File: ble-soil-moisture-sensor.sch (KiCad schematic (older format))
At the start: 29 parts, among them P1 CONN_02X03, Q1 Q_NMOS_GSD, Q2 Q_PMOS_GSD, Q3 Q_PMOS_GSD, U1 BGM111, U2 TPS78225

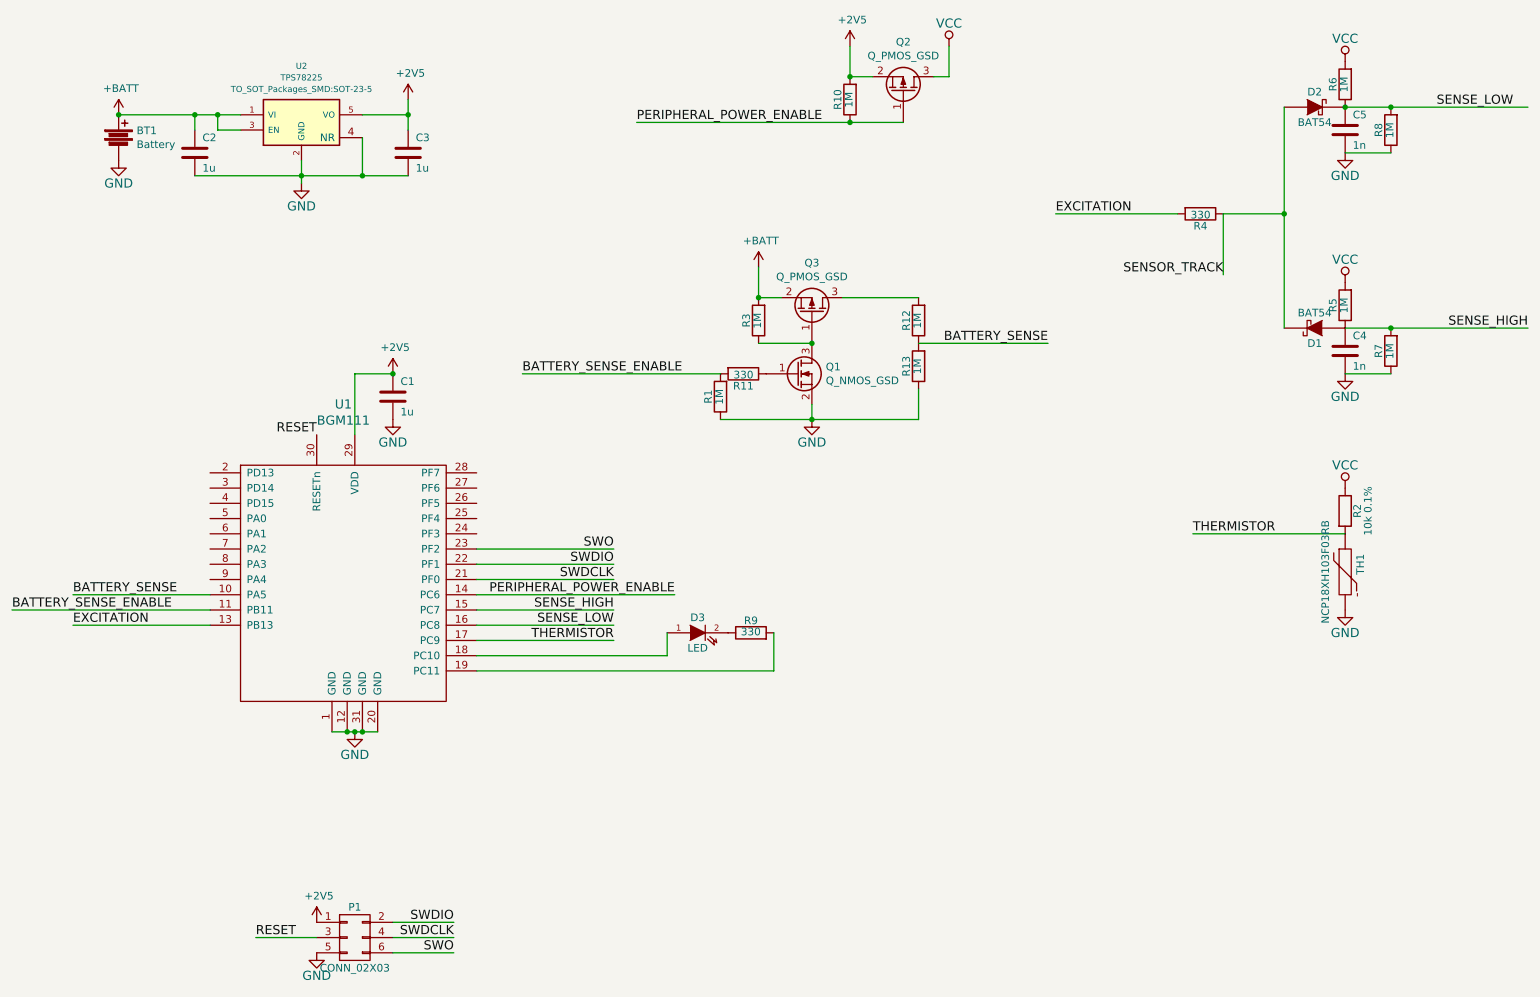
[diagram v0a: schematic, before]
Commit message: Add some fogotten schematics and pcb changes. Add BOM and firmware
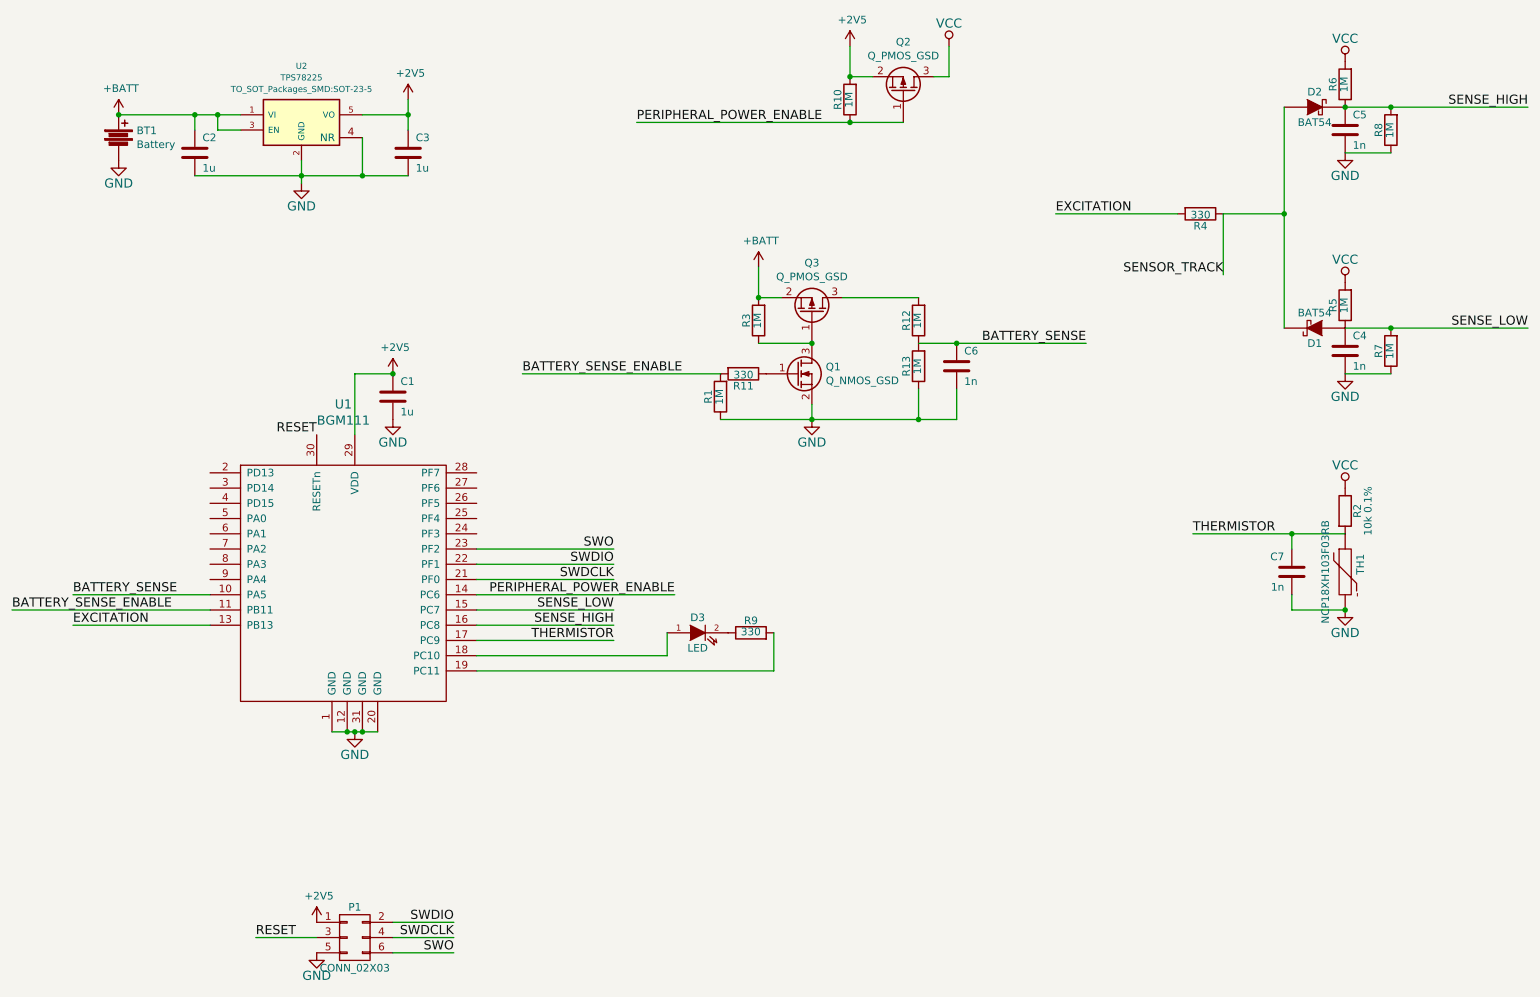
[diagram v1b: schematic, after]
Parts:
- added C6, C7: 1n, Capacitors_SMD:C_0603, symbol C
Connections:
- net BATTERY_SENSE: now also C6.1
- net GND: now also C6.2, C7.2
- net SENSE_HIGH: now also C5.1, D2.2 (K), R6.1, R8.2, U1.16 (PC8); no longer C4.1, D1.1 (A), R5.1, R7.2, U1.15 (PC7)
- net SENSE_LOW: now also C4.1, D1.1 (A), R5.1, R7.2, U1.15 (PC7); no longer C5.1, D2.2 (K), R6.1, R8.2, U1.16 (PC8)
- net THERMISTOR: now also C7.1
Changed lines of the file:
@@
 LIBS:valves
 LIBS:ble-soil-moisture-sensor-cache
-EELAYER 25 0
+EELAYER 26 0
 EELAYER END
 $Descr A4 11693 8268
@@
 $EndDescr
 $Comp
-L GND #PWR01
+L GND #PWR6
 U 1 1 581AF84C
 P 2900 5400
-F 0 "#PWR01" H 2900 5150 60  0001 C CNN
+F 0 "#PWR6" H 2900 5150 60  0001 C CNN
 F 1 "GND" H 2900 5250 60  0000 C CNN
 F 2 "" H 2900 5400 60  0000 C CNN
@@
 $EndComp
 $Comp
-L GND #PWR02
+L GND #PWR8
 U 1 1 581AF84E
 P 3150 3350
-F 0 "#PWR02" H 3150 3100 60  0001 C CNN
+F 0 "#PWR8" H 3150 3100 60  0001 C CNN
 F 1 "GND" H 3150 3200 60  0000 C CNN
 F 2 "" H 3150 3350 60  0000 C CNN
@@
 $EndComp
 $Comp
-L VCC #PWR03
+L VCC #PWR14
 U 1 1 581AF852
 P 9400 1000
-F 0 "#PWR03" H 9400 850 60  0001 C CNN
+F 0 "#PWR14" H 9400 850 60  0001 C CNN
 F 1 "VCC" H 9400 1150 60  0000 C CNN
 F 2 "" H 9400 1000 60  0000 C CNN
@@
 $EndComp
 $Comp
-L GND #PWR04
+L GND #PWR17
 U 1 1 581AF855
 P 9400 3050
-F 0 "#PWR04" H 9400 2800 60  0001 C CNN
+F 0 "#PWR17" H 9400 2800 60  0001 C CNN
 F 1 "GND" H 9400 2900 60  0000 C CNN
 F 2 "" H 9400 3050 60  0000 C CNN
@@
 $EndComp
 $Comp
-L GND #PWR05
+L GND #PWR15
 U 1 1 581AF857
 P 9400 1600
-F 0 "#PWR05" H 9400 1350 60  0001 C CNN
+F 0 "#PWR15" H 9400 1350 60  0001 C CNN
 F 1 "GND" H 9400 1450 60  0000 C CNN
 F 2 "" H 9400 1600 60  0000 C CNN
@@
 	-1   0    0    1
 $EndComp
-Text Label 10000 1300 0    60   ~ 0
+Text Label 10600 2750 2    60   ~ 0
 SENSE_LOW
 $Comp
@@
 $EndComp
 $Comp
-L VCC #PWR06
+L VCC #PWR16
 U 1 1 581AF85B
 P 9400 2450
-F 0 "#PWR06" H 9400 2300 60  0001 C CNN
+F 0 "#PWR16" H 9400 2300 60  0001 C CNN
 F 1 "VCC" H 9400 2600 60  0000 C CNN
 F 2 "" H 9400 2450 60  0000 C CNN
@@
 	1    0    0    -1
 $EndComp
-Text Label 10600 2750 2    60   ~ 0
+Text Label 10600 1300 2    60   ~ 0
 SENSE_HIGH
 Text Label 8600 2400 2    60   ~ 0
 SENSOR_TRACK
 $Comp
-L GND #PWR07
+L GND #PWR5
 U 1 1 581AF85C
 P 2650 6850
-F 0 "#PWR07" H 2650 6600 60  0001 C CNN
+F 0 "#PWR5" H 2650 6600 60  0001 C CNN
 F 1 "GND" H 2650 6700 60  0000 C CNN
 F 2 "" H 2650 6850 60  0000 C CNN
@@
 	1    0    0    -1
 $EndComp
-Text Label 4600 4600 2    60   ~ 0
+Text Label 4600 4700 2    60   ~ 0
 SENSE_HIGH
 Text Label 1050 4700 0    60   ~ 0
@@
 Text Label 7500 2000 0    60   ~ 0
 EXCITATION
-Text Label 4600 4700 2    60   ~ 0
+Text Label 4600 4600 2    60   ~ 0
 SENSE_LOW
 $Comp
@@
 $EndComp
 $Comp
-L GND #PWR08
+L GND #PWR19
 U 1 1 581AF863
 P 9400 4600
-F 0 "#PWR08" H 9400 4350 60  0001 C CNN
+F 0 "#PWR19" H 9400 4350 60  0001 C CNN
 F 1 "GND" H 9400 4450 60  0000 C CNN
 F 2 "" H 9400 4600 60  0000 C CNN
@@
 $EndComp
 $Comp
-L VCC #PWR09
+L VCC #PWR18
 U 1 1 581AF864
 P 9400 3800
-F 0 "#PWR09" H 9400 3650 60  0001 C CNN
+F 0 "#PWR18" H 9400 3650 60  0001 C CNN
 F 1 "VCC" H 9400 3950 60  0000 C CNN
 F 2 "" H 9400 3800 60  0000 C CNN
@@
 $EndComp
 Wire Wire Line
-	9400 1300 9700 1300
-Wire Wire Line
-	9700 1300 10600 1300
+	9400 1300 10600 1300
 Wire Wire Line
 	9700 1600 9400 1600
@@
 	9400 3050 9700 3050
 Wire Wire Line
-	9400 2750 9700 2750
-Wire Wire Line
-	9700 2750 10600 2750
+	9400 2750 10600 2750
 Connection ~ 9700 2750
 Wire Wire Line
-	9000 1300 9000 2000
-Wire Wire Line
-	9000 2000 9000 2750
+	9000 1300 9000 2750
 Wire Wire Line
 	8600 2000 9000 2000
@@
 RESET
 Wire Wire Line
-	2750 5400 2850 5400
-Wire Wire Line
-	2850 5400 2900 5400
-Wire Wire Line
-	2900 5400 2950 5400
-Wire Wire Line
-	2950 5400 3050 5400
+	2750 5400 3050 5400
 Connection ~ 2850 5400
 Connection ~ 2900 5400
@@
 $EndComp
 $Comp
-L GND #PWR010
+L GND #PWR2
 U 1 1 581B1E00
 P 1350 1650
-F 0 "#PWR010" H 1350 1400 60  0001 C CNN
+F 0 "#PWR2" H 1350 1400 60  0001 C CNN
 F 1 "GND" H 1350 1500 60  0000 C CNN
 F 2 "" H 1350 1650 60  0000 C CNN
@@
 $EndComp
 Wire Wire Line
-	1350 1350 1850 1350
-Wire Wire Line
-	1850 1350 2000 1350
-Wire Wire Line
-	2000 1350 2150 1350
+	1350 1350 2150 1350
 Wire Wire Line
 	2150 1450 2000 1450
@@
 Connection ~ 2000 1350
 $Comp
-L GND #PWR011
+L GND #PWR3
 U 1 1 581B1FF8
 P 2550 1800
-F 0 "#PWR011" H 2550 1550 60  0001 C CNN
+F 0 "#PWR3" H 2550 1550 60  0001 C CNN
 F 1 "GND" H 2550 1650 60  0000 C CNN
 F 2 "" H 2550 1800 60  0000 C CNN
@@
 Connection ~ 1850 1350
 Wire Wire Line
-	1850 1750 2550 1750
-Wire Wire Line
-	2550 1750 2950 1750
-Wire Wire Line
-	2950 1750 3250 1750
-Wire Wire Line
-	2550 1650 2550 1750
-Wire Wire Line
-	2550 1750 2550 1800
+	1850 1750 3250 1750
+Wire Wire Line
+	2550 1650 2550 1800
 Connection ~ 2550 1750
 Wire Wire Line
 	2950 1350 3250 1350
 Wire Wire Line
-	3250 1250 3250 1350
-Wire Wire Line
-	3250 1350 3250 1450
+	3250 1250 3250 1450
 Connection ~ 3250 1350
 $Comp
-L +2V5 #PWR012
+L +2V5 #PWR9
 U 1 1 581B2B34
 P 3250 1250
-F 0 "#PWR012" H 3250 1100 50  0001 C CNN
+F 0 "#PWR9" H 3250 1100 50  0001 C CNN
 F 1 "+2V5" H 3265 1423 50  0000 C CNN
 F 2 "" H 3250 1250 60  0000 C CNN
@@
 $EndComp
 $Comp
-L +2V5 #PWR013
+L +2V5 #PWR7
 U 1 1 581B2C05
 P 3150 3050
-F 0 "#PWR013" H 3150 2900 50  0001 C CNN
+F 0 "#PWR7" H 3150 2900 50  0001 C CNN
 F 1 "+2V5" H 3165 3223 50  0000 C CNN
 F 2 "" H 3150 3050 60  0000 C CNN
@@
 $EndComp
 $Comp
-L +2V5 #PWR014
+L +2V5 #PWR4
 U 1 1 581B307C
 P 2650 6650
-F 0 "#PWR014" H 2650 6500 50  0001 C CNN
+F 0 "#PWR4" H 2650 6500 50  0001 C CNN
 F 1 "+2V5" H 2665 6823 50  0000 C CNN
 F 2 "" H 2650 6650 60  0000 C CNN
@@
 	6300 1100 6150 1100
 $Comp
-L +2V5 #PWR015
+L +2V5 #PWR12
 U 1 1 581B370E
 P 6150 900
-F 0 "#PWR015" H 6150 750 50  0001 C CNN
+F 0 "#PWR12" H 6150 750 50  0001 C CNN
 F 1 "+2V5" H 6165 1073 50  0000 C CNN
 F 2 "" H 6150 900 60  0000 C CNN
@@
 Connection ~ 6150 1100
 Wire Wire Line
-	4750 1400 6150 1400
-Wire Wire Line
-	6150 1400 6500 1400
+	4750 1400 6500 1400
 $Comp
 L Q_NMOS_GSD Q1
@@
 $EndComp
 $Comp
-L GND #PWR016
+L GND #PWR11
 U 1 1 581B3F2F
 P 5900 3350
-F 0 "#PWR016" H 5900 3100 60  0001 C CNN
+F 0 "#PWR11" H 5900 3100 60  0001 C CNN
 F 1 "GND" H 5900 3200 60  0000 C CNN
 F 2 "" H 5900 3350 60  0000 C CNN
@@
 $EndComp
 Wire Wire Line
-	5300 3350 5900 3350
-Wire Wire Line
-	5900 3350 6600 3350
+	5300 3350 6850 3350
 Wire Wire Line
 	5900 3350 5900 3250
 Connection ~ 5900 3350
 $Comp
-L VCC #PWR017
+L VCC #PWR13
 U 1 1 581B4128
 P 6800 900
-F 0 "#PWR017" H 6800 750 60  0001 C CNN
+F 0 "#PWR13" H 6800 750 60  0001 C CNN
 F 1 "VCC" H 6800 1050 60  0000 C CNN
 F 2 "" H 6800 900 60  0000 C CNN
@@
 Connection ~ 2950 1750
 $Comp
-L +BATT #PWR018
+L +BATT #PWR1
 U 1 1 581B79D2
 P 1350 1350
-F 0 "#PWR018" H 1350 1200 50  0001 C CNN
+F 0 "#PWR1" H 1350 1200 50  0001 C CNN
 F 1 "+BATT" H 1365 1523 50  0000 C CNN
 F 2 "" H 1350 1350 60  0000 C CNN
@@
 Connection ~ 5900 2850
 $Comp
-L +BATT #PWR019
+L +BATT #PWR10
 U 1 1 5824CC8F
 P 5550 2350
-F 0 "#PWR019" H 5550 2200 50  0001 C CNN
+F 0 "#PWR10" H 5550 2200 50  0001 C CNN
 F 1 "+BATT" H 5565 2523 50  0000 C CNN
 F 2 "" H 5550 2350 60  0000 C CNN
@@
 	6600 3350 6600 3150
 Wire Wire Line
-	6600 2850 7450 2850
-Text Label 7450 2850 2    60   ~ 0
+	6600 2850 7700 2850
+Text Label 7700 2850 2    60   ~ 0
 BATTERY_SENSE
 Wire Wire Line
@@
 Text Label 1050 4500 0    60   ~ 0
 BATTERY_SENSE
+$Comp
+L C C6
+U 1 1 583E0E4B
+P 6850 3000
+F 0 "C6" H 6900 3100 50  0000 L CNN
+F 1 "1n" H 6900 2900 50  0000 L CNN
+F 2 "Capacitors_SMD:C_0603" H 6888 2850 30  0001 C CNN
+F 3 "" H 6850 3000 60  0000 C CNN
+F 4 " MC0603B102K500CT" H 6850 3000 60  0001 C CNN "PartNo"
+F 5 "MULTICOMP" H 6850 3000 60  0001 C CNN "Manufacturer"
+F 6 "Farnell/2310598" H 6850 3000 60  0001 C CNN "Distributor"
+	1    6850 3000
+	1    0    0    -1
+$EndComp
+Wire Wire Line
+	6850 3350 6850 3150
+Connection ~ 6600 3350
+Connection ~ 6850 2850
+$Comp
+L C C7
+U 1 1 583E128B
+P 9050 4350
+F 0 "C7" H 9100 4450 50  0000 L CNN
+F 1 "1n" H 9100 4250 50  0000 L CNN
+F 2 "Capacitors_SMD:C_0603" H 9088 4200 30  0001 C CNN
+F 3 "" H 9050 4350 60  0000 C CNN
+F 4 " MC0603B102K500CT" H 9050 4350 60  0001 C CNN "PartNo"
+F 5 "MULTICOMP" H 9050 4350 60  0001 C CNN "Manufacturer"
+F 6 "Farnell/2310598" H 9050 4350 60  0001 C CNN "Distributor"
+	1    9050 4350
+	-1   0    0    -1
+$EndComp
+Wire Wire Line
+	9050 4500 9050 4600
+Wire Wire Line
+	9050 4600 9400 4600
+Connection ~ 9400 4600
+Wire Wire Line
+	9050 4200 9050 4100
+Connection ~ 9050 4100
 $EndSCHEMATC
